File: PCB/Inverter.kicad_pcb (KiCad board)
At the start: 2 copper layers, 71.4 x 105.7 mm, 77 parts, among them J1 Conn_01x02_Socket, J3 Conn_01x05_Pin, J4 Conn_01x05_Pin, J5 Conn_01x03_Socket, Q1 STP60NF06, Q2 STP60NF06, Q3 STP60NF06, Q4 STP60NF06, Q5 STP60NF06, Q6 STP60NF06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

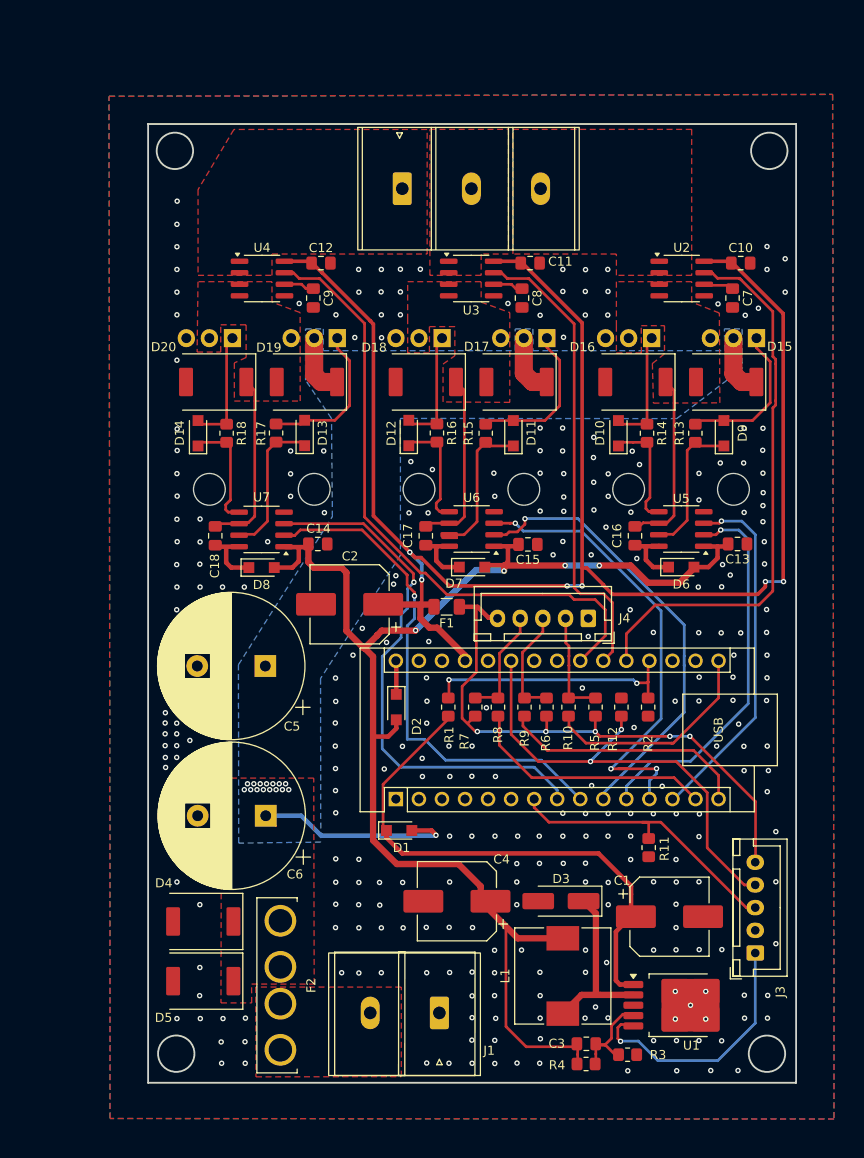
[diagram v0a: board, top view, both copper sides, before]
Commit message: Change#007
Add OSHW logo and PCB 3d model in step format
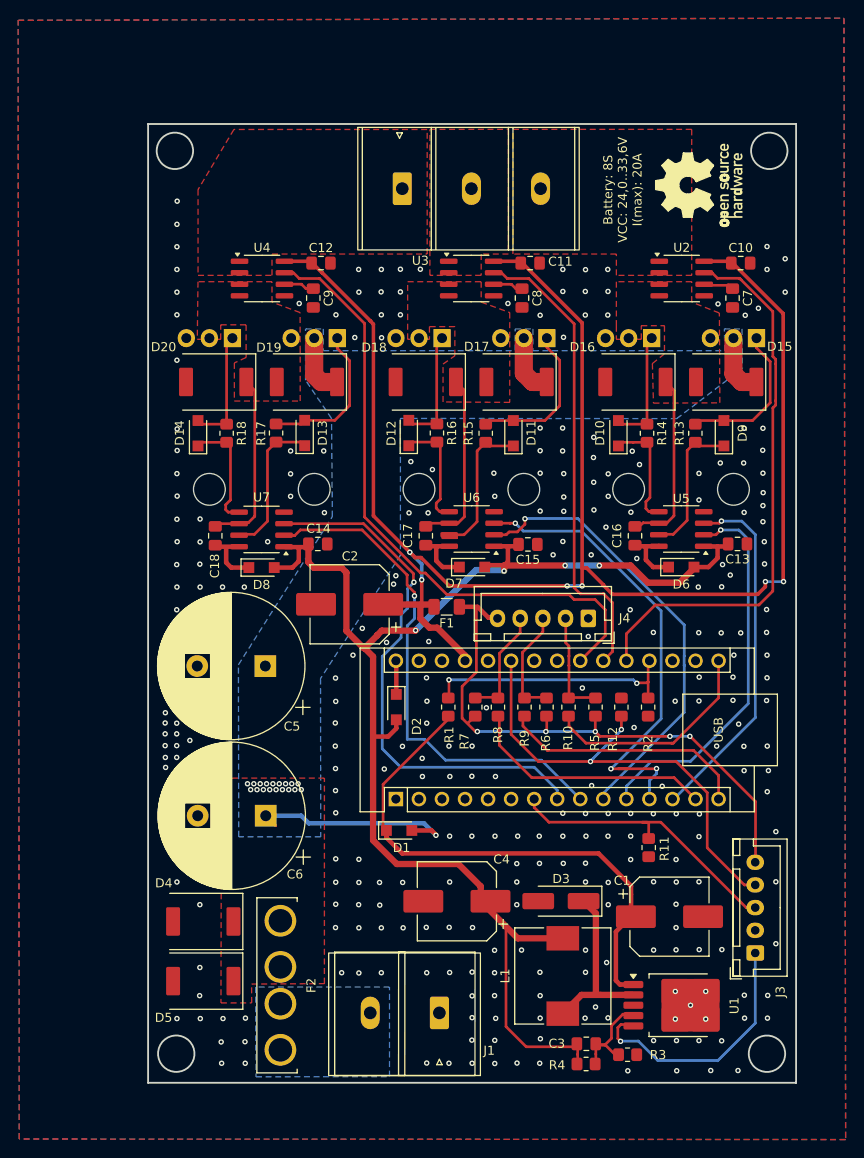
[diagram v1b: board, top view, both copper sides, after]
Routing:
- net +33V: track 43.1 -> 43.0 mm, vias 16 -> 19
- added copper zone on B.Cu, net /Vin
- removed copper zone on F.Cu, net /Vin
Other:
- board text added: "Battery: 8S VCC: 24,0..33,6V I(max): 20A"
- board text added: "github.com/techn0man1ac/SimpleBLDC"
